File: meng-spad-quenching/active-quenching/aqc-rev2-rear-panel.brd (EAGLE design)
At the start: 78 x 27 mm, 2 parts, among them X1 HAMMOND_1455J1201_SIDE_PANEL

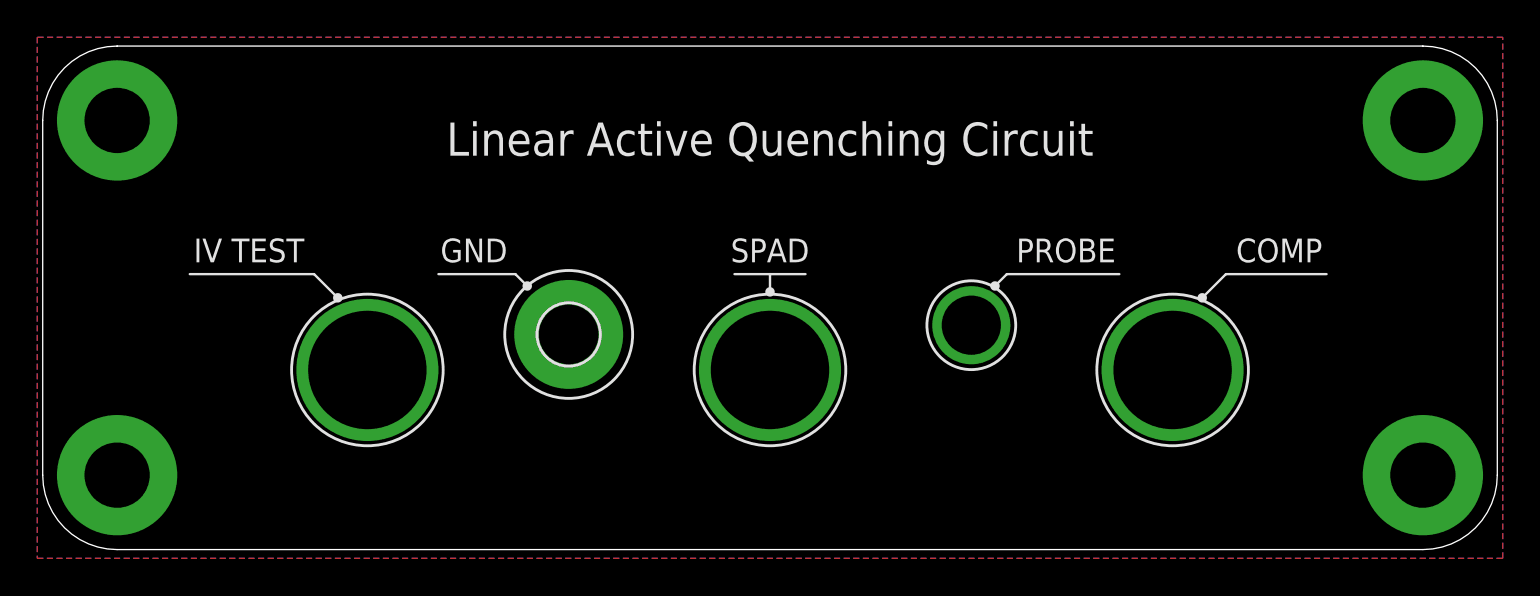
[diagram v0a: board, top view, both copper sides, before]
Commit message: Made front and rear PCBs, exported gerbers for first rev
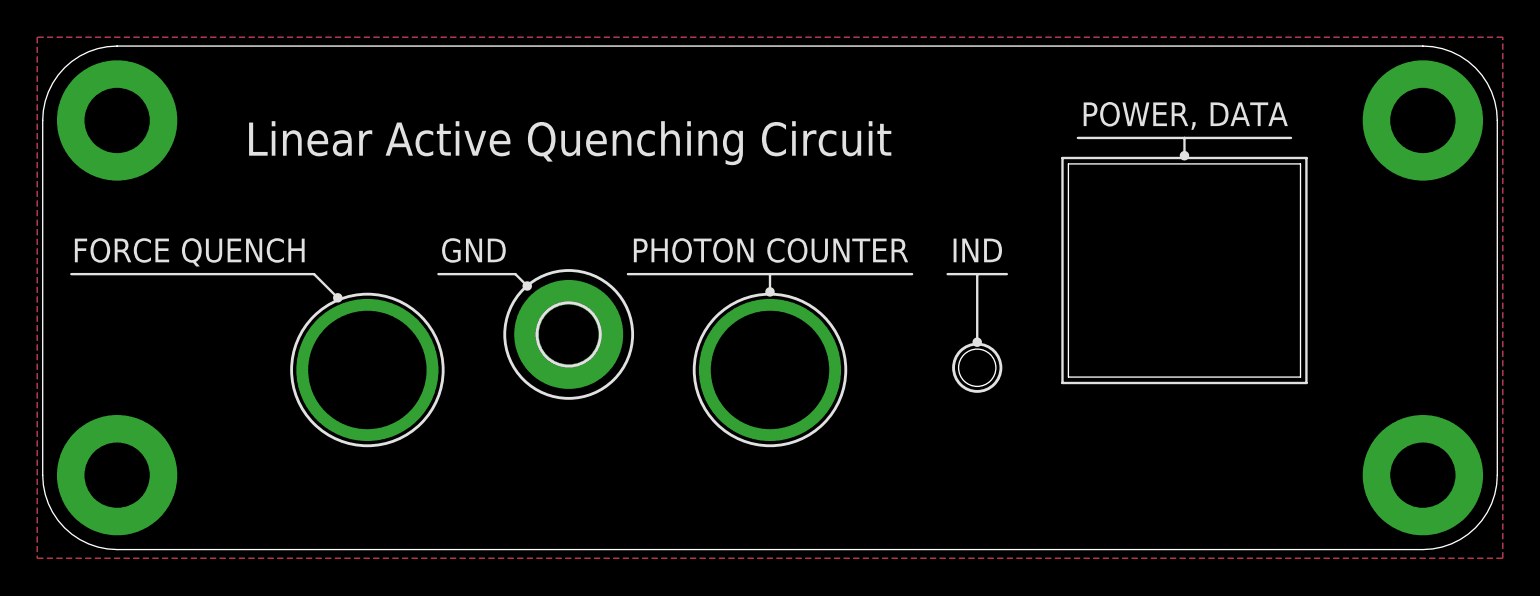
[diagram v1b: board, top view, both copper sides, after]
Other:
- board text added: "FORCE QUENCH"
- board text added: "IND"
- board text added: "PHOTON COUNTER"
- board text added: "POWER, DATA"
- board text removed: "COMP"
- board text removed: "IV TEST"
- board text removed: "PROBE"
- board text removed: "SPAD"
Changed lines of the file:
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@@
 <setting verticaltext="up"/>
 </settings>
-<grid distance="5" unitdist="mm" unit="mm" style="lines" multiple="1" display="yes" altdistance="5" altunitdist="mil" altunit="mil"/>
+<grid distance="0.0125" unitdist="inch" unit="inch" style="lines" multiple="1" display="yes" altdistance="5" altunitdist="mil" altunit="mil"/>
 <layers>
 <layer number="1" name="Top" color="4" fill="1" visible="yes" active="yes"/>
@@
 <board>
 <plain>
-<text x="-27.94" y="1.905" size="1.27" layer="25" align="bottom-center">IV TEST</text>
-<text x="0" y="1.905" size="1.27" layer="25" align="bottom-center">SPAD</text>
-<text x="27.305" y="1.905" size="1.27" layer="25" align="bottom-center">COMP</text>
-<text x="15.875" y="1.905" size="1.27" layer="25" align="bottom-center">PROBE</text>
-<text x="0" y="7.62" size="1.778" layer="25" align="bottom-center">Linear Active Quenching Circuit</text>
+<text x="-31.115" y="1.905" size="1.27" layer="25" align="bottom-center">FORCE QUENCH</text>
+<text x="0" y="1.905" size="1.27" layer="25" align="bottom-center">PHOTON COUNTER</text>
+<text x="-10.795" y="7.62" size="1.778" layer="25" align="bottom-center">Linear Active Quenching Circuit</text>
 <text x="-15.875" y="1.905" size="1.27" layer="25" align="bottom-center">GND</text>
 <circle x="-21.59" y="-3.868928125" radius="4.064" width="0.1524" layer="21"/>
 <circle x="0" y="-3.868928125" radius="4.064" width="0.1524" layer="21"/>
-<circle x="21.59" y="-3.868928125" radius="4.064" width="0.1524" layer="21"/>
-<circle x="10.795" y="-1.468628125" radius="2.38125" width="0.1524" layer="21"/>
 <circle x="-23.1775" y="0" radius="0.127" width="0.254" layer="21"/>
 <wire x1="-23.1775" y1="0" x2="-24.4475" y2="1.27" width="0.127" layer="21"/>
-<wire x1="-24.4475" y1="1.27" x2="-31.115" y2="1.27" width="0.127" layer="21"/>
+<wire x1="-24.4475" y1="1.27" x2="-37.465" y2="1.27" width="0.127" layer="21"/>
 <circle x="-13.0175" y="0.635" radius="0.127" width="0.254" layer="21"/>
 <circle x="0" y="0.3175" radius="0.127" width="0.254" layer="21"/>
-<circle x="12.065" y="0.635" radius="0.127" width="0.254" layer="21"/>
-<circle x="23.1775" y="0" radius="0.127" width="0.254" layer="21"/>
 <wire x1="-13.0175" y1="0.635" x2="-13.6525" y2="1.27" width="0.127" layer="21"/>
 <wire x1="-13.6525" y1="1.27" x2="-17.78" y2="1.27" width="0.127" layer="21"/>
-<wire x1="-1.905" y1="1.27" x2="0" y2="1.27" width="0.127" layer="21"/>
-<wire x1="0" y1="1.27" x2="1.905" y2="1.27" width="0.127" layer="21"/>
+<wire x1="-7.62" y1="1.27" x2="0" y2="1.27" width="0.127" layer="21"/>
 <wire x1="0" y1="0.3175" x2="0" y2="1.27" width="0.127" layer="21"/>
-<wire x1="24.4475" y1="1.27" x2="23.1775" y2="0" width="0.127" layer="21"/>
-<wire x1="29.845" y1="1.27" x2="24.4475" y2="1.27" width="0.127" layer="21"/>
-<wire x1="12.7" y1="1.27" x2="12.065" y2="0.635" width="0.127" layer="21"/>
-<wire x1="18.7325" y1="1.27" x2="12.7" y2="1.27" width="0.127" layer="21"/>
 <polygon width="0.3048" layer="30">
 <vertex x="-38.9725" y="-13.6525"/>
@@
 <vertex x="38.9725" y="-13.6525"/>
 </polygon>
+<wire x1="16.002" y1="7.180071875" x2="16.002" y2="-4.249928125" width="0" layer="20"/>
+<wire x1="16.002" y1="-4.249928125" x2="28.448" y2="-4.249928125" width="0" layer="20"/>
+<wire x1="28.448" y1="-4.249928125" x2="28.448" y2="7.180071875" width="0" layer="20"/>
+<wire x1="28.448" y1="7.180071875" x2="16.002" y2="7.180071875" width="0" layer="20"/>
+<wire x1="0" y1="1.27" x2="7.62" y2="1.27" width="0.127" layer="21"/>
+<wire x1="15.6845" y1="-4.567428125" x2="15.6845" y2="7.497571875" width="0.127" layer="21"/>
+<wire x1="28.7655" y1="7.497571875" x2="15.6845" y2="7.497571875" width="0.127" layer="21"/>
+<wire x1="28.7655" y1="-4.567428125" x2="28.7655" y2="7.497571875" width="0.127" layer="21"/>
+<wire x1="28.7655" y1="-4.567428125" x2="15.6845" y2="-4.567428125" width="0.127" layer="21"/>
+<text x="22.225" y="9.2075" size="1.27" layer="25" align="bottom-center">POWER, DATA</text>
+<circle x="22.225" y="7.62" radius="0.127" width="0.254" layer="21"/>
+<wire x1="22.225" y1="7.62" x2="22.225" y2="8.5725" width="0.127" layer="21"/>
+<wire x1="16.51" y1="8.5725" x2="22.225" y2="8.5725" width="0.127" layer="21"/>
+<wire x1="22.225" y1="8.5725" x2="27.94" y2="8.5725" width="0.127" layer="21"/>
+<hole x="11.1125" y="-3.75" drill="2"/>
+<circle x="11.1125" y="-3.75" radius="1.27" width="0.1524" layer="21"/>
+<circle x="11.1125" y="-2.38125" radius="0.127" width="0.254" layer="21"/>
+<wire x1="11.1125" y1="-2.54" x2="11.1125" y2="1.27" width="0.127" layer="21"/>
+<text x="11.1125" y="1.905" size="1.27" layer="25" align="bottom-center">IND</text>
+<wire x1="11.1125" y1="1.27" x2="12.7" y2="1.27" width="0.127" layer="21"/>
+<wire x1="9.525" y1="1.27" x2="11.1125" y2="1.27" width="0.127" layer="21"/>
 </plain>
 <attributes>
@@
 </polygon>
 <via x="0" y="-3.868928125" extent="1-16" drill="6.35" diameter="7.62"/>
-<via x="21.59" y="-3.868928125" extent="1-16" drill="6.35" diameter="7.62"/>
 <contactref element="H1" pad="B3,2"/>
-<via x="10.795" y="-1.468628125" extent="1-16" drill="3.175"/>
 </signal>
 </signals>
